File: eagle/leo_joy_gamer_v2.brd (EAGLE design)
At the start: 80 x 47.1 mm, 50 parts, among them IC3 MAX6520, J1 AVR_SPI_PRG, U1 ATMEGA32U4, U3 JOYSTICKPTH, U4 microSD, U5 MCP73831, X2 USB-MICROB

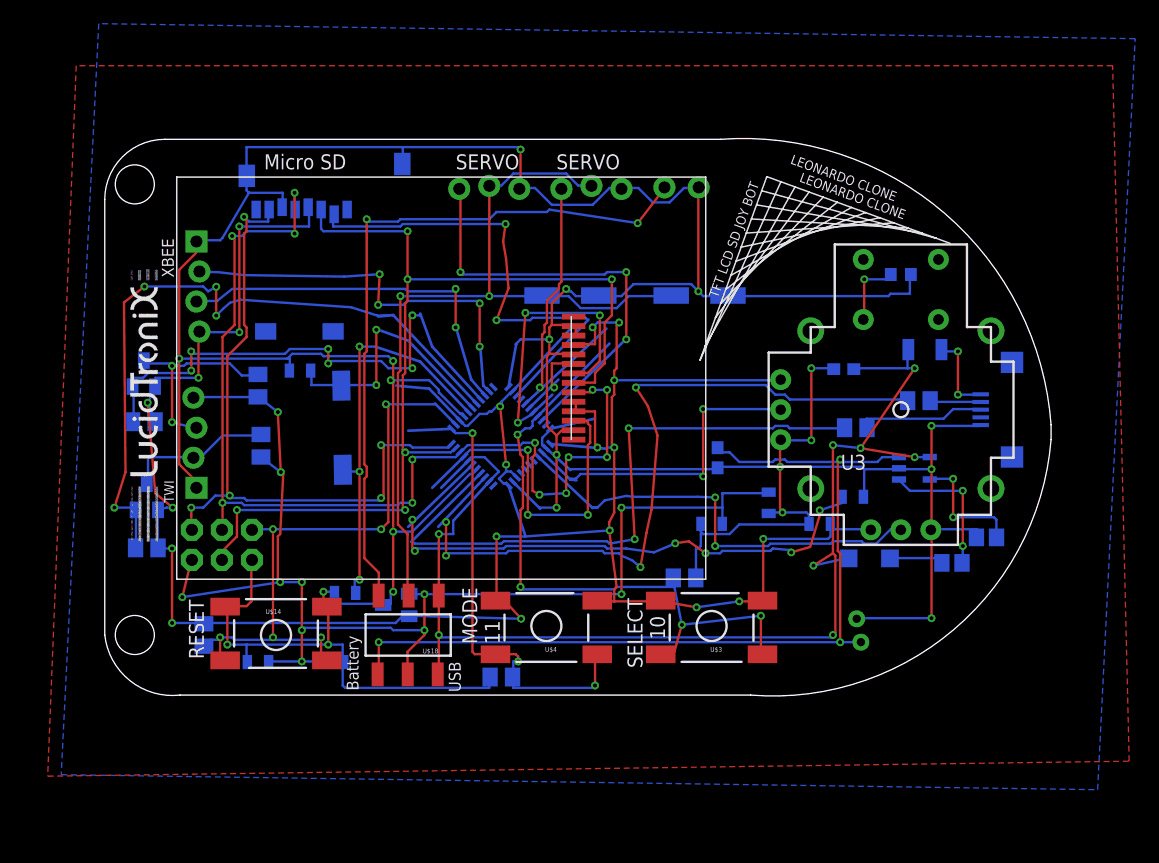
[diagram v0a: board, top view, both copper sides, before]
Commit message: added meshes and eagle CAD
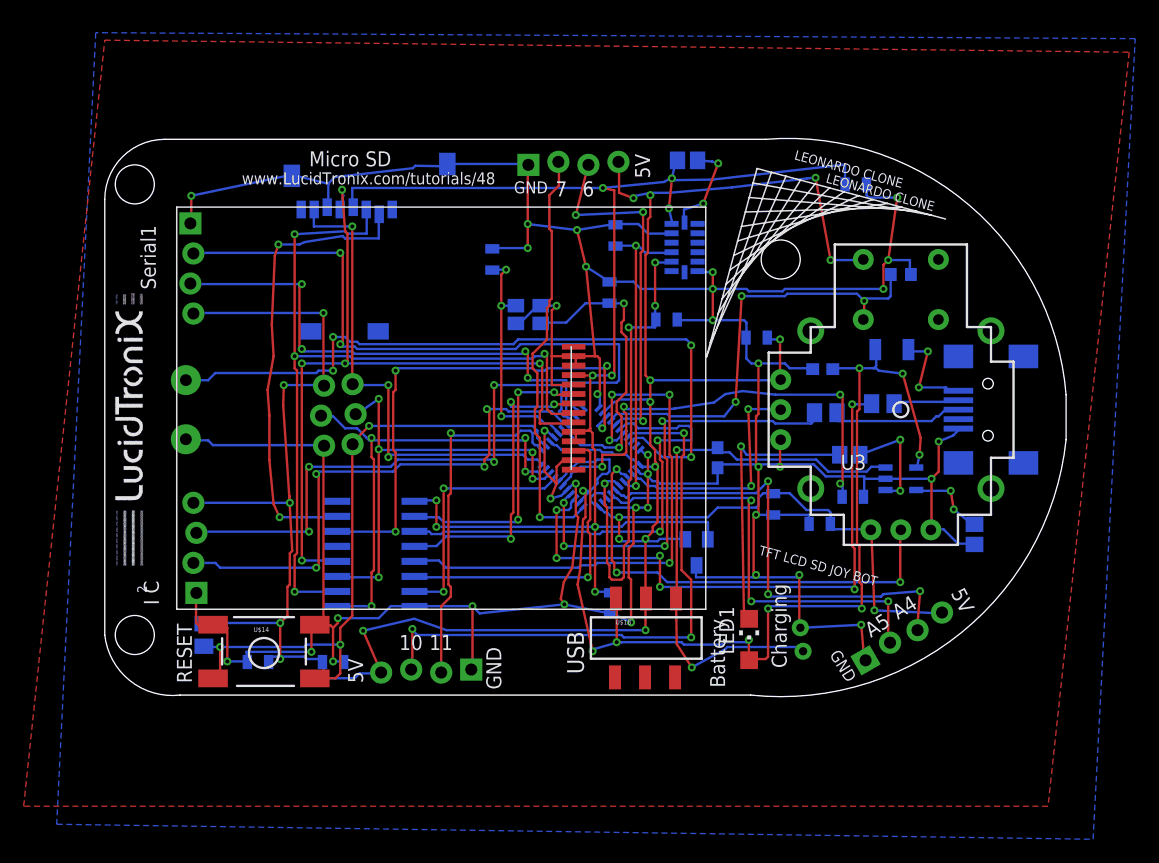
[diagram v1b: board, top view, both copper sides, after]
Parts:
- removed J1: AVR_SPI_PRG, SparkFun:2X3
- removed R10: 2.2K, resistor:M0805
- removed R3, R4: 10k, resistor:M0805
- removed R7, R8: 2.7K, resistor:M0805
- removed SERVO1, SERVO2: (no value), SparkFun:1X03_LOCK
- removed TRANSISTAH1, TRANSISTAH2: TRANSISTOR_MOSFET_N, sam:SOT23
- removed TWI, XBEE: (no value), SparkFun:1X04_LOCK
- removed U$1: CRYSTAL, sam:CRYSTAL_SMD
- removed U$3, U$4: TAC_SWITCHSMD, sam:TAC_SWITCH_SMD
- removed X2: USB-MICROB, SparkFun:USB-MICROB
- added C14: 3300pf, SparkFun:0805
- added C15: 0.1uf, SparkFun:0805
- added I2C, SERIAL, SERIAL1, STEP1, STEP2: (no value), SparkFun:1X04_LOCK
- added JP3: STAND-OFF, SparkFun:STAND-OFF
- added JP5: (no value), SparkFun:1X03_LOCK
- added SP1: SPEAKER/PS12, adafruit:PS12
- added U$12: ACCELEROMETER_MMA6331L, sam:LGA14
- added U$2: CD4050SO_16_MIDDLE, sam:SO_16
- added U$25: CRYSTAL_4PAD, sam:CRYSTAL_4PAD_TINY
- added X1: USBSMD, SparkFun:USB-MINIB
- C10: value (none) -> 3300pf; device resistor:PANASONIC_D -> SparkFun:0805
- C9: value (none) -> 10uf; device resistor:PANASONIC_D -> SparkFun:0805
- JP1: device SparkFun:1X02_LOCK -> SparkFun:1X03_LOCK
- R9: value 2.2k -> 10k; device resistor:M0805 -> resistor:R0805
- moved R9 43.4 mm to (49.3, 45.2), turned to 180 degrees
- moved JP1 36.4 mm to (18.4, 21.1), turned to 90 degrees
- moved C3 30.8 mm to (32.8, 36.8), turned to 270 degrees
- moved C2 27.0 mm to (42.7, 34.0), turned to 270 degrees
- moved C9 26.3 mm to (42.8, 7.75), turned to 270 degrees
- moved IC3 25.8 mm to (50.0, 12.1), turned to 180 degrees
- moved U$18 20.1 mm to (45.7, 4.83), turned to 0 degrees
- moved C5 16.2 mm to (55.1, 30.2)
- moved R13 12.6 mm to (63.0, 20.3)
- moved LED1 12.3 mm to (54.5, 4.70), flipped to the top, turned to 0 degrees
- moved U1 7.82 mm to (41.1, 20.1)
- moved JP6 4.89 mm to (58.9, 4.70), turned to 263.4 degrees
- moved U4 3.81 mm to (15.4, 30.4)
- moved C10 3.45 mm to (47.5, 31.8)
- moved R2 3.06 mm to (65.8, 24.6)
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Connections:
- removed net +7V: C10.+, C9.+, SERVO1.2, SERVO2.2, U$18.10
- removed net PD7: R6.2, U3.B2A
- removed net PE6: U1.1
- removed net PF1_A4: U1.40
- removed net RST: J1.5, R5.1, U$14.3, U$14.4, U1.13
- removed net SCL_3V3: R7.2, TRANSISTAH2.2, U1.18
- removed net SDA_3V3: R8.2, TRANSISTAH1.2, U1.19
- removed net VDD: JP1.1, U$18.11
- new net MOSI_3V3: LCD1.8, U$2.10, U4.3
- new net N$10: R9.2, U$12.7
- new net N$4: LCD1.7, U$2.4
- new net N$5: LCD1.12, U$2.6
- new net N$7: U$2.15, U4.2
- new net PE6_7: STEP1.2, U1.1
- new net PF0: STEP2.2, U1.41
- new net PF1: STEP2.3, U1.40
- new net RESET: JP5.3, R5.1, U$14.3, U$14.4, U1.13
- new net SCK_3V3: LCD1.9, U$2.12, U4.5
- net +3V3: now also C15.2, C9.1, R9.1, U$12.6, U$2.1; no longer C1.1, R5.2, R7.1, R8.1, TRANSISTAH1.1, TRANSISTAH2.1, U$3.3, U$3.4, U$4.3, U$4.4, U1.14, U1.24, U1.34, U1.42, U1.44, U3.H1, U3.V1, XBEE.4
- net 5V: now also C1.1, I2C.4, JP1.3, R5.2, SERIAL.4, SERIAL1.4, STEP1.4, STEP2.4, U1.14, U1.24, U1.34, U1.42, U1.44, U3.B1A, U3.H1, U3.V1; no longer J1.2, R10.1, R9.1, TWI.4
- net CS: now also U$2.14; no longer U4.2
- net D+: now also X1.D+; no longer X2.D+
- net D-: now also X1.D-; no longer X2.D-
- net GND: now also C10.1, C14.1, C15.1, C9.2, I2C.1, JP1.1, SERIAL.1, SERIAL1.1, SP1.P$2, STEP1.1, STEP2.1, U$12.13, U$12.5, U$2.8, U$25.2, U$25.4, X1.GND; no longer C10.-, C9.-, J1.6, JP1.2, R3.2, R4.2, SERVO1.3, SERVO2.3, TWI.1, X2.GND, XBEE.1
- net MISO: now also JP5.1; no longer J1.1
- net MOSI: now also JP1.2, U$2.9; no longer J1.4, LCD1.8, U4.3
- net N$1: now also LCD1.6, U$2.2; no longer U3.B1A
- net N$2: now also U$25.3; no longer U$1.2
- net N$3: now also U$25.1; no longer U$1.1
- net PB0: now also U$2.7; no longer LCD1.12
- net PB4_8: now also U$2.3; no longer LCD1.6
- net PB5_9: now also U$2.5; no longer LCD1.7
- net PB6_10: now also SERIAL1.3; no longer R3.1, U$3.1, U$3.2
- net PB7_11: now also SERIAL1.2; no longer R4.1, U$4.1, U$4.2
- net PC6_5: now also SP1.P$1; no longer SERVO1.1
- net PD2: now also SERIAL.3; no longer XBEE.3
- net PD3: now also SERIAL.2; no longer XBEE.2
- net PD6_12: now also R6.2, U3.B2A
- net PD7_6: now also STEP1.3; no longer SERVO2.1
- net PF4: now also C10.2, U$12.2
- net PF5: now also C14.2, U$12.3
- net SCK: now also JP5.2, U$2.11; no longer J1.3, LCD1.9, U4.5
- net SCL: now also I2C.2, U1.18; no longer R9.2, TRANSISTAH2.3, TWI.2
- net SDA: now also I2C.3, U1.19; no longer R10.2, TRANSISTAH1.3, TWI.3
- net VBUS: now also X1.VBUS; no longer X2.VBUS
- net VCC: no longer U$18.9
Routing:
- net 5V: track 107.4 -> 247.4 mm, vias 11 -> 19
- net +3V3: track 221.7 -> 122.3 mm, vias 20 -> 9
- net MOSI_3V3: track 0.00 -> 70.9 mm, vias 0 -> 4
- net +7V: track 68.4 -> 0.00 mm, vias 2 -> 0
- net SCK_3V3: track 0.00 -> 64.6 mm, vias 0 -> 5
- net SCL_3V3: track 60.7 -> 0.00 mm, vias 4 -> 0
- net VDD: track 59.9 -> 0.00 mm, vias 2 -> 0
- net RESET: track 0.00 -> 55.2 mm, vias 0 -> 3
- net RST: track 53.3 -> 0.00 mm, vias 6 -> 0
- net SCK: track 88.8 -> 38.0 mm, vias 13 -> 5
- net SDA_3V3: track 45.5 -> 0.00 mm, vias 6 -> 0
- net MOSI: track 85.0 -> 40.8 mm, vias 6 -> 4
- net PF4: track 0.00 -> 41.6 mm, vias 0 -> 4
- net PF1: track 0.00 -> 39.7 mm, vias 0 -> 3
- net N$7: track 0.00 -> 38.9 mm, vias 0 -> 2
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- added copper zone on layer 1, net 5V
- removed copper zone on layer 1, net +3V3
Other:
- board size 80 x 47.1 mm -> 81.3 x 47.2 mm
- board text added: "12"
- board text added: "16MHz"
- board text added: "3300pf"
- board text added: "6331"
- board text added: "7"
- board text added: "A0"
- board text added: "A1"
- board text added: "A4"
- board text added: "A5"
- board text added: "AccelerometerX->3"
- board text added: "AccelerometerY->2"
- board text added: "Atmega"
- board text added: "CD4050"
- board text added: "I C"
- board text added: "JoyBtn->12"
- board text added: "JoyX->1"
- board text added: "JoyY->0"
- board text added: "MMA"
- board text added: "Mini"
- board text added: "PIEZO"
- board text added: "Piezo PWM 5"
- board text added: "Serial1"
- board text added: "www.LucidTronix.com/tutorials/48"
- board text removed: "100uf"
- board text removed: "138"
- board text removed: "2.2k"
- board text removed: "2.7K"
- board text removed: "3V3"
- board text removed: "3v3 Only"
- board text removed: "5"
- board text removed: "7V"
- board text removed: "BSS"
- board text removed: "C"
- board text removed: "I"
- board text removed: "MODE"
- board text removed: "MOSFET"
- board text removed: "Micro"
- board text removed: "Motor"
- board text removed: "RST"
- board text removed: "SELECT"
- board text removed: "SERVO"
- board text removed: "TWI"
- board text removed: "XBEE"
- board text removed: "atmega"
